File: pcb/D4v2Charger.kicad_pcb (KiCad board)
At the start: 2 copper layers, 17 x 14 mm, 15 parts, among them J1 Conn_01x02_Pin, U1 BQ25185DLHR

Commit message: 3dFootprint updates
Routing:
- net GND: track 1.49 -> 2.44 mm
- net (no net): vias 0 -> 13
- added copper zone on B.Cu, net GND
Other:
- board text added: "D4V2 Charger Sandwich board"

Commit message: updated step file & re-import
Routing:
- net GND: vias 0 -> 5
- net (no net): vias 13 -> 0
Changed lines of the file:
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@@
 		)
 	)
-	(via
-		(at 152 92)
+	(segment
+		(start 142.802064 88.3)
+		(end 143.5 87.602064)
+		(width 0.2)
+		(layer "F.Cu")
+		(net 1)
+	)
+	(segment
+		(start 143.5 87.602064)
+		(end 143.5 87.5)
+		(width 0.1)
+		(layer "F.Cu")
+		(net 1)
+	)
+	(segment
+		(start 142.4 88.4)
+		(end 143 89)
+		(width 0.2)
+		(layer "F.Cu")
+		(net 1)
+	)
+	(segment
+		(start 142.4 88.3)
+		(end 142.802064 88.3)
+		(width 0.2)
+		(layer "F.Cu")
+		(net 1)
+	)
+	(segment
+		(start 142.4 88.3)
+		(end 142.4 88.4)
+		(width 0.2)
+		(layer "F.Cu")
+		(net 1)
+	)
+	(via
+		(at 150 98.5)
 		(size 0.5)
 		(drill 0.3)
 		(layers "F.Cu" "B.Cu")
+		(free yes)
 		(tenting none)
-		(net 0)
-	)
-	(via
-		(at 149.5 87)
+		(net 1)
+	)
+	(via
+		(at 152 93)
 		(size 0.5)
 		(drill 0.3)
 		(layers "F.Cu" "B.Cu")
+		(free yes)
 		(tenting none)
-		(net 0)
-	)
-	(via
-		(at 151 97)
+		(net 1)
+	)
+	(via
+		(at 143.5 84.5)
 		(size 0.5)
 		(drill 0.3)
 		(layers "F.Cu" "B.Cu")
+		(free yes)
 		(tenting none)
-		(net 0)
-	)
-	(via
-		(at 151 89)
-		(size 0.5)
-		(drill 0.3)
-		(layers "F.Cu" "B.Cu")
-		(tenting none)
-		(net 0)
+		(net 1)
 	)
 	(via
@@
 		(drill 0.3)
 		(layers "F.Cu" "B.Cu")
+		(free yes)
 		(tenting none)
-		(net 0)
-	)
-	(via
-		(at 151.5 96)
+		(net 1)
+	)
+	(via
+		(at 135 93)
 		(size 0.5)
 		(drill 0.3)
 		(layers "F.Cu" "B.Cu")
+		(free yes)
 		(tenting none)
-		(net 0)
-	)
-	(via
-		(at 152 93)
-		(size 0.5)
-		(drill 0.3)
-		(layers "F.Cu" "B.Cu")
-		(tenting none)
-		(net 0)
-	)
-	(via
-		(at 136 97)
-		(size 0.5)
-		(drill 0.3)
-		(layers "F.Cu" "B.Cu")
-		(tenting none)
-		(net 0)
-	)
-	(via
-		(at 152 94)
-		(size 0.5)
-		(drill 0.3)
-		(layers "F.Cu" "B.Cu")
-		(tenting none)
-		(net 0)
-	)
-	(via
-		(at 150 98.5)
-		(size 0.5)
-		(drill 0.3)
-		(layers "F.Cu" "B.Cu")
-		(tenting none)
-		(net 0)
-	)
-	(via
-		(at 151.5 90)
-		(size 0.5)
-		(drill 0.3)
-		(layers "F.Cu" "B.Cu")
-		(tenting none)
-		(net 0)
-	)
-	(via
-		(at 149 86.5)
-		(size 0.5)
-		(drill 0.3)
-		(layers "F.Cu" "B.Cu")
-		(tenting none)
-		(net 0)
-	)
-	(via
-		(at 150 87.5)
-		(size 0.5)
-		(drill 0.3)
-		(layers "F.Cu" "B.Cu")
-		(tenting none)
-		(net 0)
-	)
-	(segment
-		(start 142.802064 88.3)
-		(end 143.5 87.602064)
-		(width 0.2)
-		(layer "F.Cu")
-		(net 1)
-	)
-	(segment
-		(start 143.5 87.602064)
-		(end 143.5 87.5)
-		(width 0.1)
-		(layer "F.Cu")
-		(net 1)
-	)
-	(segment
-		(start 142.4 88.4)
-		(end 143 89)
-		(width 0.2)
-		(layer "F.Cu")
-		(net 1)
-	)
-	(segment
-		(start 142.4 88.3)
-		(end 142.802064 88.3)
-		(width 0.2)
-		(layer "F.Cu")
-		(net 1)
-	)
-	(segment
-		(start 142.4 88.3)
-		(end 142.4 88.4)
-		(width 0.2)
-		(layer "F.Cu")
 		(net 1)
 	)
@@
 	)
 	(segment
-		(start 141.725001 97.5)
-		(end 142.225001 97)
+		(start 142.225 97.5)
+		(end 138.983 97.5)
 		(width 0.4)
 		(layer "F.Cu")
-		(net 13)
-	)
-	(segment
-		(start 138.983 97.5)
-		(end 141.725001 97.5)
-		(width 0.4)
-		(layer "F.Cu")

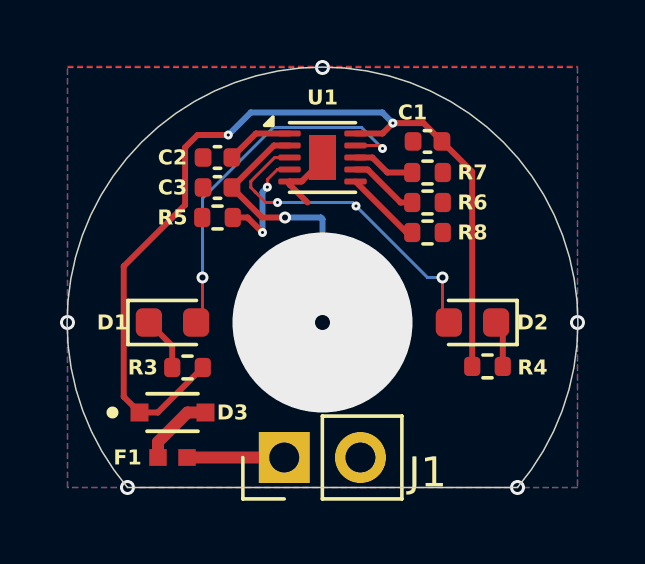
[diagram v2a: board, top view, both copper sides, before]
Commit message: update pcb with spring contact for battery +
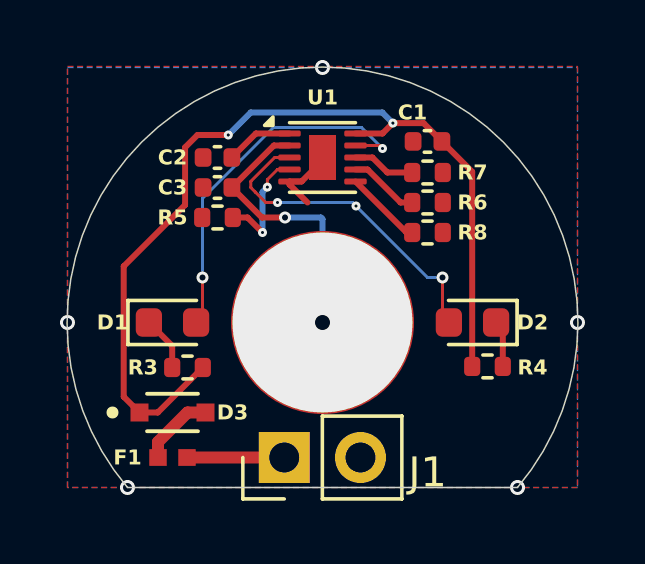
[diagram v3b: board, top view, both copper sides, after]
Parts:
- added TP1: Flashlight_+, Custom_TestPoints:TestPoint_Pad_D6.0mm_spring, F.Cu at (143.5, 93.0)
- D3: value D_Schottky -> 60V, 1A cont.
- F1: value Polyfuse -> 1A hold, 2A trip
- R7: value 560Ω -> 390Ω
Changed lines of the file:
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@@
 	(net 13 "Net-(J1-Pin_1)")
 	(net 14 "Net-(U1-SYS)")
+	(footprint "Custom_TestPoints:TestPoint_Pad_D6.0mm_spring"
+		(layer "F.Cu")
+		(at 143.5 93)
+		(property "Reference" "TP1"
+			(at 0 -4 0)
+			(unlocked yes)
+			(layer "F.SilkS")
+			(hide yes)
+			(effects
+				(font
+					(size 1 1)
+					(thickness 0.1)
+				)
+			)
+		)
+		(property "Value" "Flashlight_+"
+			(at 0 6 0)
+			(unlocked yes)
+			(layer "F.Fab")
+			(hide yes)
+			(effects
+				(font
+					(size 1 1)
+					(thickness 0.15)
+				)
+			)
+		)
+		(property "Datasheet" ""
+			(at 0 0 0)
+			(unlocked yes)
+			(layer "F.Fab")
+			(hide yes)
+			(effects
+				(font
+					(size 1 1)
+					(thickness 0.15)
+				)
+			)
+		)
+		(property "Description" "test point"
+			(at 0 0 0)
+			(unlocked yes)
+			(layer "F.Fab")
+			(hide yes)
+			(effects
+				(font
+					(size 1 1)
+					(thickness 0.15)
+				)
+			)
+		)
+		(property ki_fp_filters "Pin* Test*")
+		(sheetname "/")
+		(sheetfile "D4v2Charger.kicad_sch")
+		(attr exclude_from_pos_files)
+		(fp_circle
+			(center 0 0)
+			(end 3 0)
+			(stroke
+				(width 0.1)
+				(type solid)
+			)
+			(fill yes)
+			(layer "F.Cu")
+		)
+		(fp_circle
+			(center 0 0)
+			(end 3 0)
+			(stroke
+				(width 0.1)
+				(type solid)
+			)
+			(fill yes)
+			(layer "F.Mask")
+		)
+		(embedded_fonts no)
+		(model "${KIPRJMOD}/TestPad_SpringModel/Spring_6mm-Body.step"
+			(offset
+				(xyz 0 0 0.5)
+			)
+			(scale
+				(xyz 1 1 1)
+			)
+			(rotate
+				(xyz -0 -0 -0)
+			)
+		)
+	)
 	(footprint "Package_DFN_QFN:Texas_DLH0010A_WSON-10-1EP_2.2x2mm_P0.4mm_EP0.9x1.5mm"
 		(layer "F.Cu")
@@
 			)
 		)
-		(property "Value" "D_Schottky"
+		(property "Value" "60V, 1A cont."
 			(at 0 1.5 0)
 			(layer "F.Fab")
@@
 			)
 		)
-		(property "Value" "560Ω"
+		(property "Value" "390Ω"
 			(at 0 1.17 0)
 			(layer "F.Fab")
@@
 			)
 		)
-		(property "Value" "Polyfuse"
+		(property "Value" "1A hold, 2A trip"
 			(at 0.5 1 0)
 			(layer "F.Fab")

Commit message: add ntcg thremistor & drc resolve
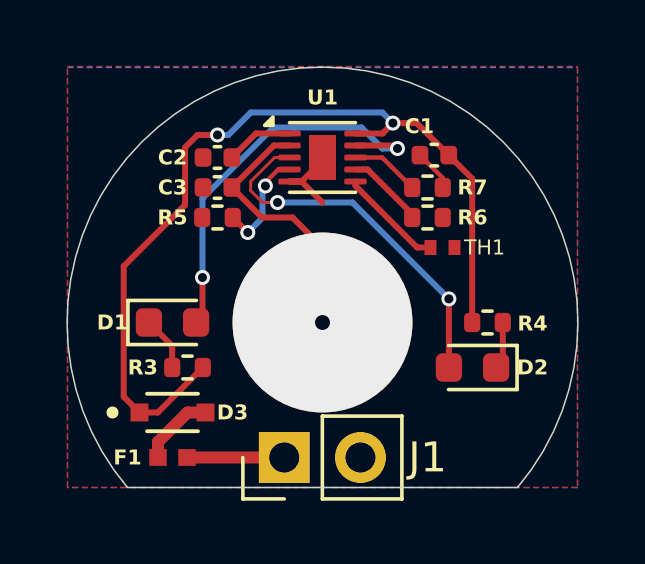
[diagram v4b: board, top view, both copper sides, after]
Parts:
- removed R8: 10kΩ, Resistor_SMD:R_0402_1005Metric
- added TH1: Thermistor, NTCG103JF103FT1:THERM_NTCG103JF103FT1, F.Cu at (147.5, 90.5)
- moved D2 1.50 mm to (148.5, 94.5)
- moved R4 1.46 mm to (149.0, 93.0)
- moved C1 0.51 mm to (147.2, 87.4)
- moved R6 0.50 mm to (147.0, 89.5)
- moved R7 0.50 mm to (147.0, 88.5)
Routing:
- net GND: track 2.44 -> 4.28 mm, vias 5 -> 0
- net VBUS: track 31.4 -> 29.8 mm
- net Net-(D2-A): track 11.0 -> 12.3 mm, vias 3 -> 2
- net Net-(D1-A): track 12.4 -> 13.4 mm
- net Net-(U1-TS/MR): track 2.59 -> 3.50 mm
- net Net-(BT1-+): track 9.40 -> 8.85 mm, vias 2 -> 1
